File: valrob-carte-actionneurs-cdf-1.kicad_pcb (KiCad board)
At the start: 4 copper layers, 50 x 50 mm, 126 parts, among them J1 USB_C_Receptacle_USB2.0_14P, J2 Conn_01x02, J3 Conn_01x02, J4 Conn_01x04_Pin, J5 Conn_01x02, J6 Conn_01x02, J7 Conn_01x12, M1 Motor_Servo, M10 Motor_Servo, M11 Motor_Servo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

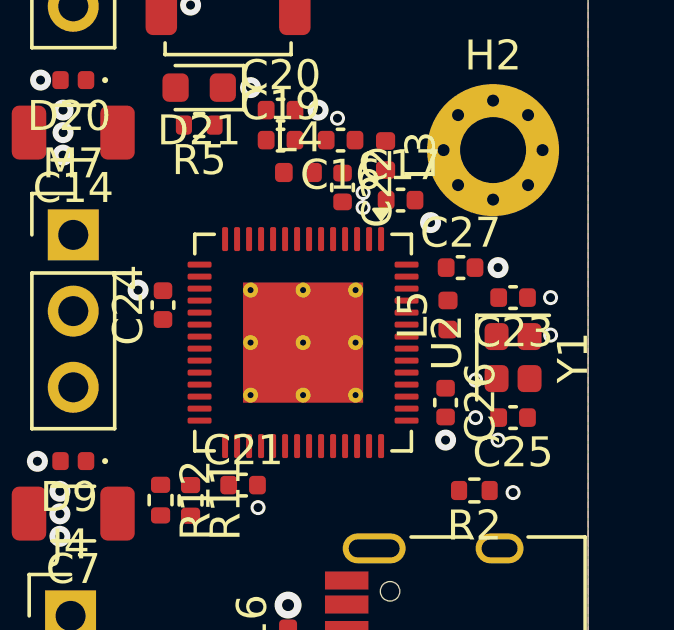
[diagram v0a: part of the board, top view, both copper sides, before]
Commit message: schem: reorganize programmable GPIOs
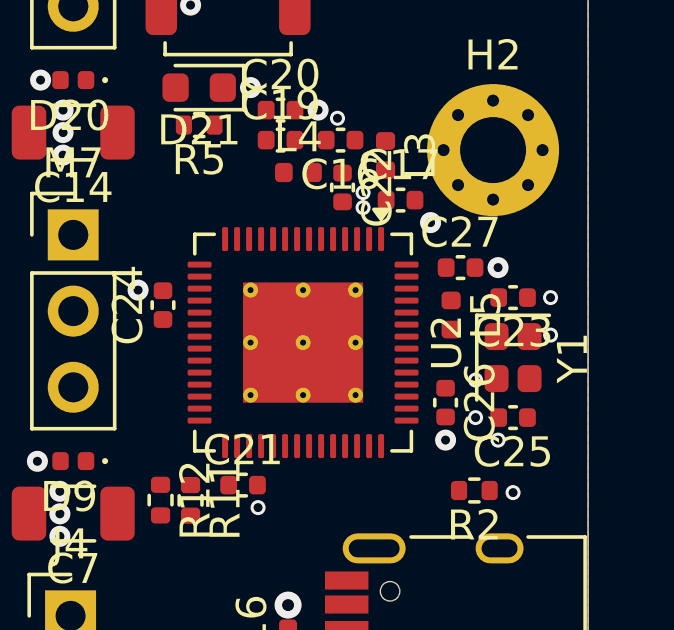
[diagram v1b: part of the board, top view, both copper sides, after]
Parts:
- moved L5 0.10 mm to (129.4, 76.3), turned to -90 degrees
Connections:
- J7 pad 1: /GPIO41 -> /GPIO48
- J7 pad 10: /GPIO15 -> /GPIO40
- J7 pad 11: /GPIO16 -> /GPIO41
- J7 pad 2: /GPIO42 -> /GPIO47
- J7 pad 8: /GPIO47 -> /GPIO38
- J7 pad 9: /GPIO48 -> /GPIO39
- U2 pad 10: /PG_B -> /SERVO10
- U2 pad 11: /SERVO1 -> /SERVO9
- U2 pad 12: /SERVO2 -> /SERVO8
- U2 pad 13: /SERVO3 -> /SERVO6
- U2 pad 14: /SERVO4 -> /SERVO7
- U2 pad 16: /SERVO6 -> /SERVO4
- U2 pad 17: /SERVO7 -> /SERVO3
- U2 pad 18: /SERVO8 -> /SERVO2
- U2 pad 19: /SERVO9 -> /SERVO1
- U2 pad 21: /GPIO15 -> /PG_B
- U2 pad 22: /GPIO16 -> /PG_A
- U2 pad 23: /SERVO10 -> /ILM_A
- U2 pad 24: /SERVO11 -> /ILM_B
- U2 pad 27: /SERVO12 -> /RGB
- U2 pad 43: /SERVO13 -> /GPIO38
- U2 pad 44: /CAN_TX -> /GPIO39
- U2 pad 45: /CAN_RX -> /GPIO40
- U2 pad 48: /GPIO42 -> /CAN_RX
- U2 pad 51: /SERVO14 -> /CAN_TX
- U2 pad 6: /RGB -> /SERVO14
- U2 pad 7: /ILM_A -> /SERVO13
- U2 pad 8: /ILM_B -> /SERVO12
- U2 pad 9: /PG_A -> /SERVO11

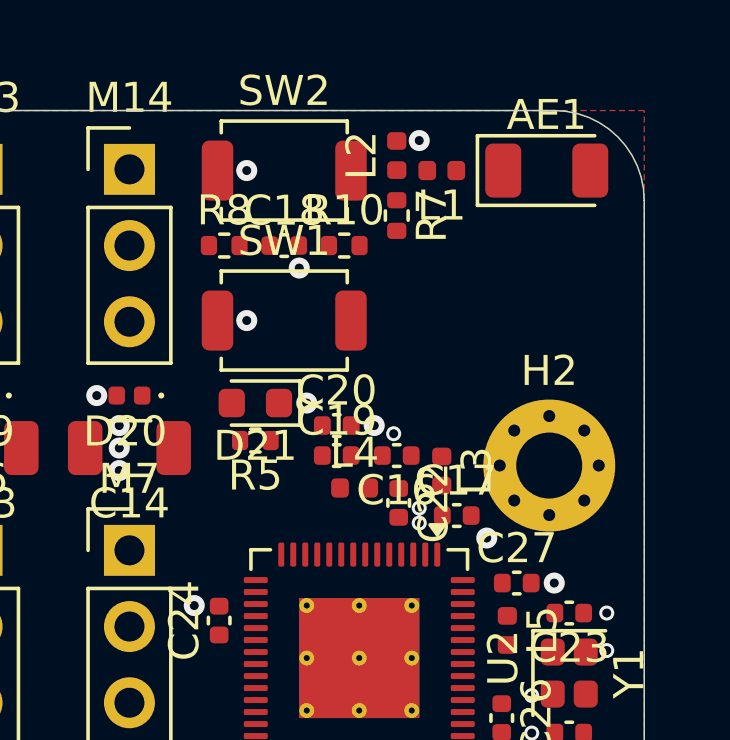
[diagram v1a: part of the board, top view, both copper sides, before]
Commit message: pcb: add rf routing
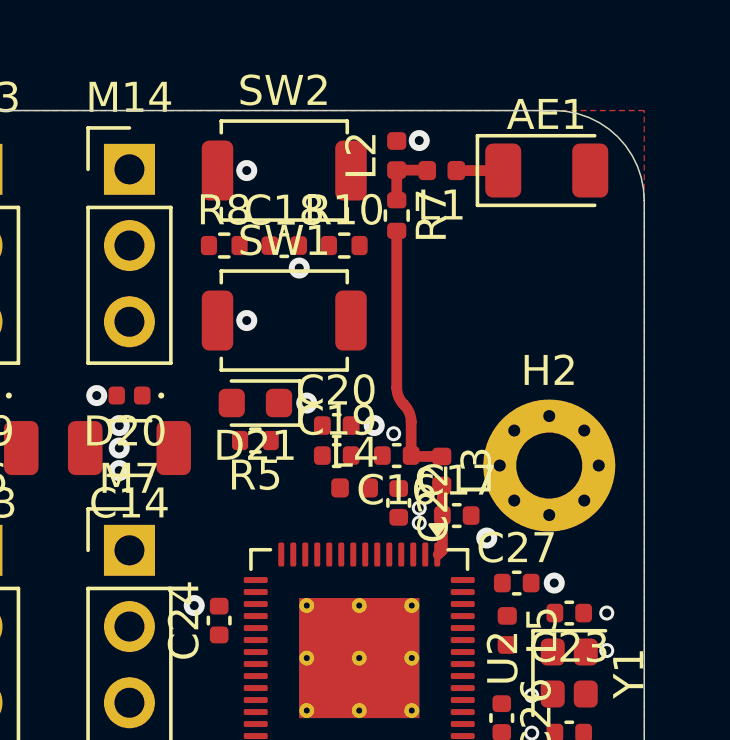
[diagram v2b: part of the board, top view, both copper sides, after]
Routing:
- net /RF_TRANS: track 0.00 -> 8.64 mm
- net /RF_ESP: track 0.00 -> 2.37 mm
- net Net-(L1-Pad2): track 0.00 -> 2.03 mm
- net /RF_ANT: track 0.00 -> 1.57 mm
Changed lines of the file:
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@@
 		(layer "Edge.Cuts")
 	)
+	(segment
+		(start 127.735 61)
+		(end 129.3 61)
+		(width 0.359)
+		(layer "F.Cu")
+		(net 1)
+	)
 	(via
 		(at 106.25 90.25)
@@
 		(net 2)
 	)
+	(segment
+		(start 126.23 70.5)
+		(end 126.23 69.376371)
+		(width 0.359)
+		(layer "F.Cu")
+		(net 4)
+	)
+	(segment
+		(start 126.26 70.53)
+		(end 126.23 70.5)
+		(width 0.359)
+		(layer "F.Cu")
+		(net 4)
+	)
+	(segment
+		(start 125.995685 68.810685)
+		(end 125.984314 68.799314)
+		(width 0.359)
+		(layer "F.Cu")
+		(net 4)
+	)
+	(segment
+		(start 127.25 70.53)
+		(end 126.26 70.53)
+		(width 0.359)
+		(layer "F.Cu")
+		(net 4)
+	)
+	(segment
+		(start 125.75 68.233629)
+		(end 125.75 63.01)
+		(width 0.359)
+		(layer "F.Cu")
+		(net 4)
+	)
+	(arc
+		(start 125.984314 68.799314)
+		(mid 125.810896 68.539775)
+		(end 125.75 68.233629)
+		(width 0.359)
+		(layer "F.Cu")
+		(net 4)
+	)
+	(arc
+		(start 126.23 69.376371)
+		(mid 126.169103 69.070224)
+		(end 125.995685 68.810685)
+		(width 0.359)
+		(layer "F.Cu")
+		(net 4)
+	)
+	(segment
+		(start 127.27 73.6605)
+		(end 127.1305 73.8)
+		(width 0.359)
+		(layer "F.Cu")
+		(net 5)
+	)
+	(segment
+		(start 127.27 71.52)
+		(end 127.25 71.5)
+		(width 0.359)
+		(layer "F.Cu")
+		(net 5)
+	)
+	(segment
+		(start 127.27 72.5)
+		(end 127.27 71.52)
+		(width 0.359)
+		(layer "F.Cu")
+		(net 5)
+	)
+	(segment
+		(start 127.27 72.5)
+		(end 127.27 73.6605)
+		(width 0.359)
+		(layer "F.Cu")
+		(net 5)
+	)
+	(segment
+		(start 126.75 60.985)
+		(end 126.765 61)
+		(width 0.359)
+		(layer "F.Cu")
+		(net 34)
+	)
+	(segment
+		(start 125.75 61.99)
+		(end 125.75 60.985)
+		(width 0.359)
+		(layer "F.Cu")
+		(net 34)
+	)
+	(segment
+		(start 125.75 60.985)
+		(end 126.75 60.985)
+		(width 0.359)
+		(layer "F.Cu")
+		(net 34)
+	)
 	(zone

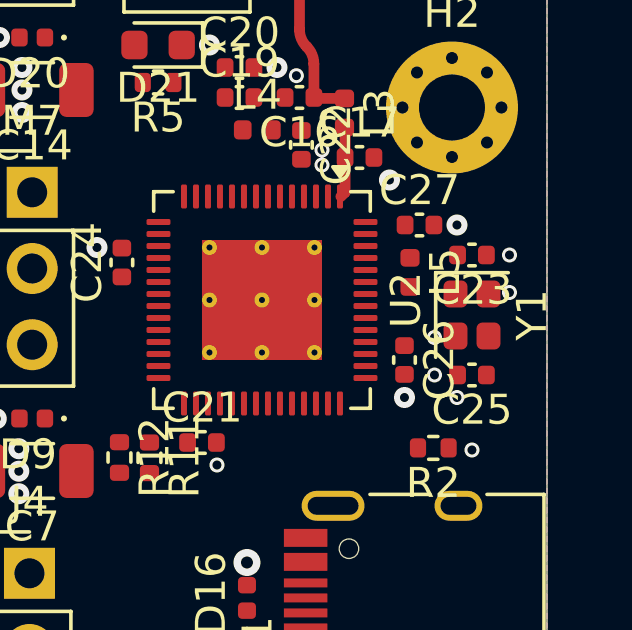
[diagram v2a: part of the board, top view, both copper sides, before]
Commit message: pcb: add crystal routing
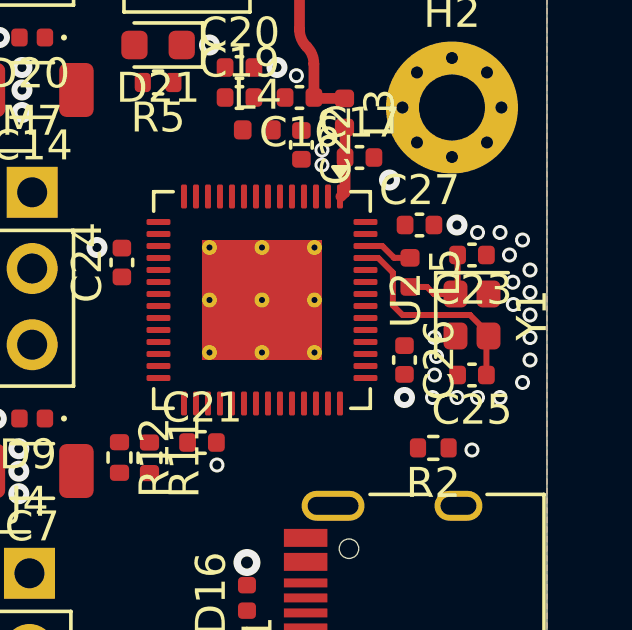
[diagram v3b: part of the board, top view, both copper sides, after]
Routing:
- net /XTAL_N: track 0.00 -> 7.20 mm
- net /XTAL_PL: track 0.00 -> 2.94 mm
- net /XTAL_P: track 0.00 -> 1.65 mm
- net GND: vias 121 -> 135

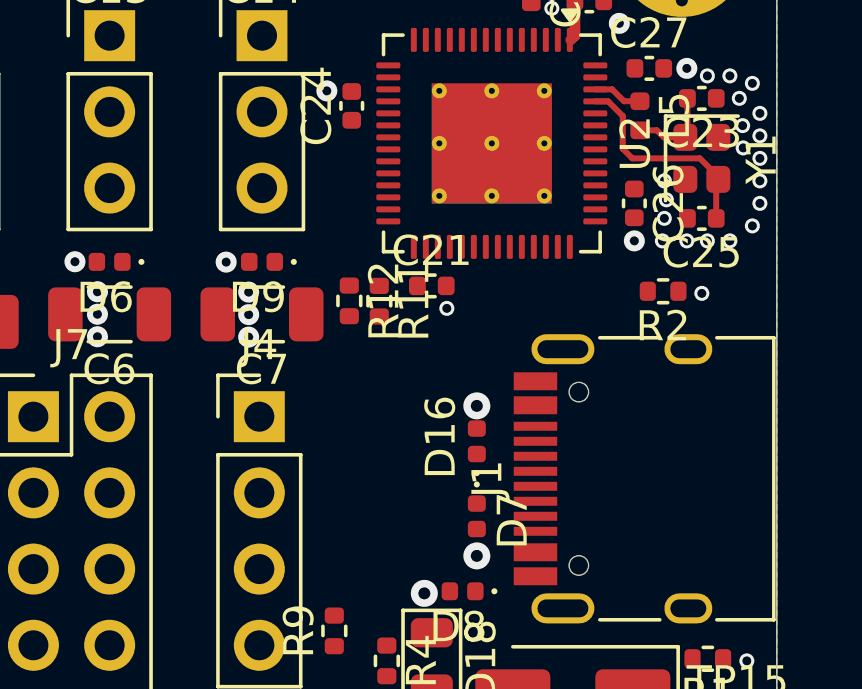
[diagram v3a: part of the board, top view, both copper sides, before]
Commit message: pcb: add usb routing
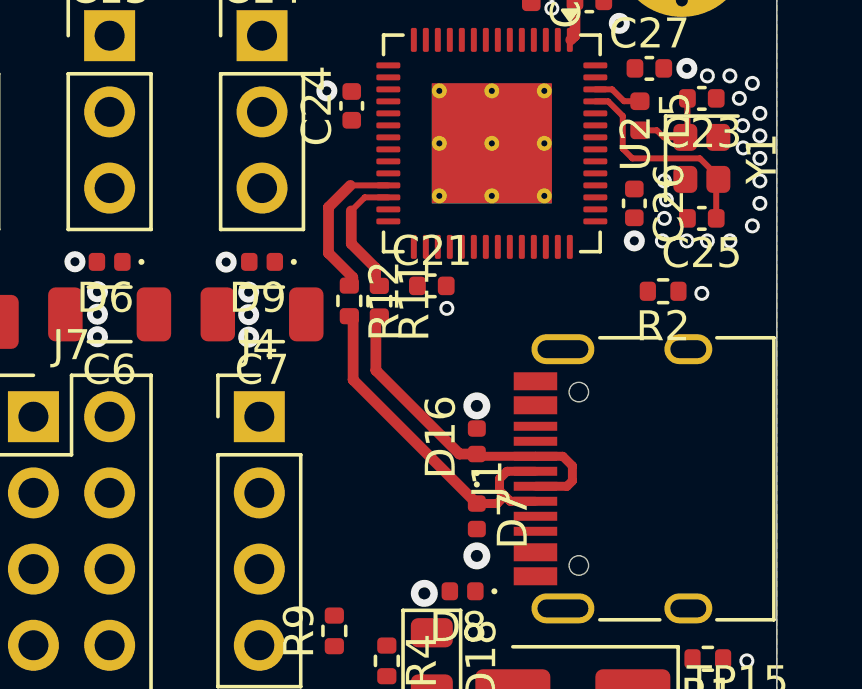
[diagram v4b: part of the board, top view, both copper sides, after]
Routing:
- net /D-: track 0.00 -> 12.1 mm
- net /D+: track 0.00 -> 11.5 mm
- net /ESP_D-: track 0.00 -> 5.29 mm
- net /ESP_D+: track 0.00 -> 4.31 mm

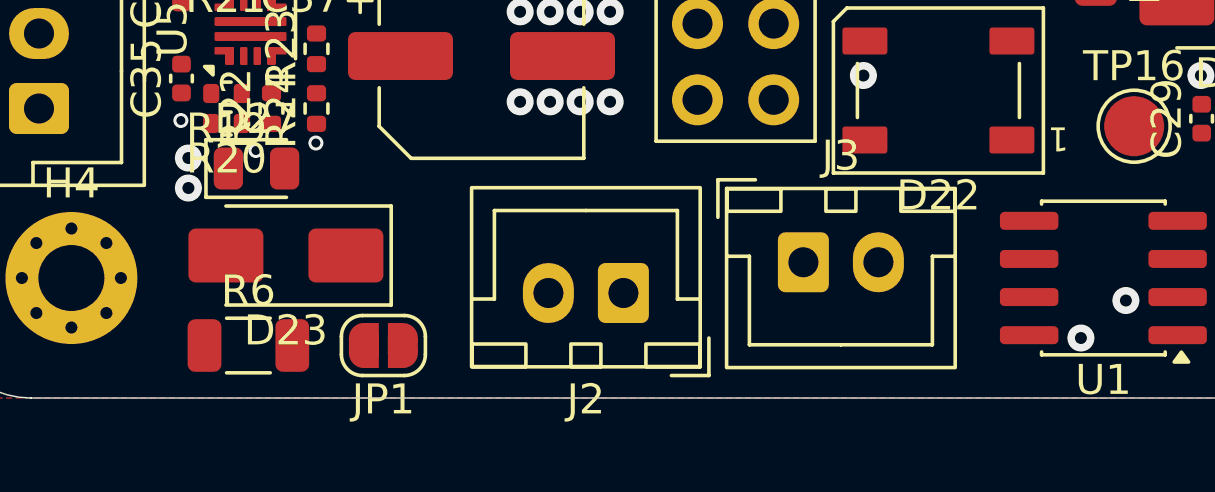
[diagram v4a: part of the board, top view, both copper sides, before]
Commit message: pcb: add can routing
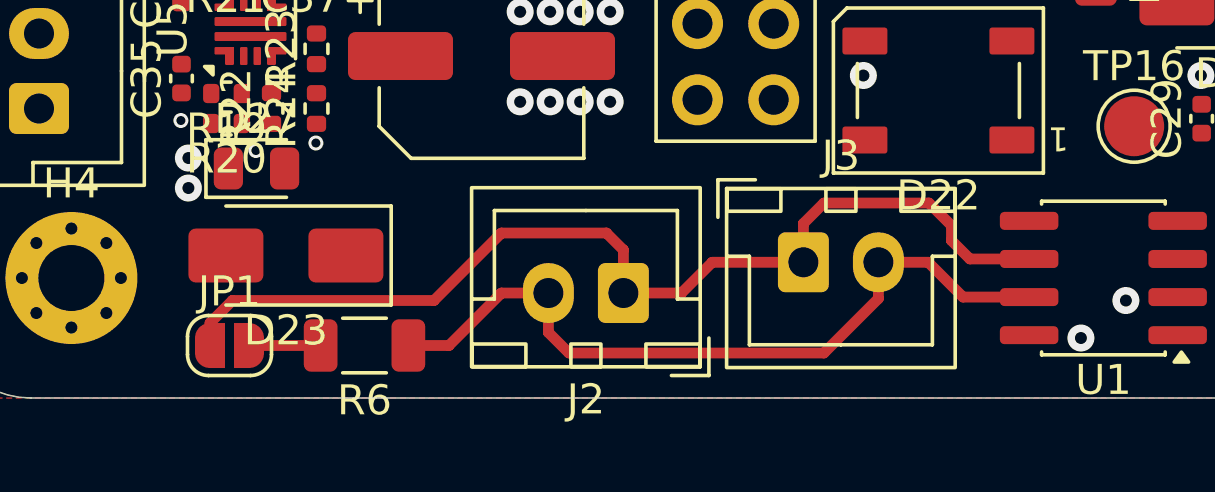
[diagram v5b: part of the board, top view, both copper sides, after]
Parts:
- moved JP1 5.13 mm to (93.6, 107.2), turned to 0 degrees
- moved R6 3.87 mm to (98.1, 107.2), turned to 180 degrees
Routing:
- net /CANL: track 0.00 -> 34.0 mm
- net /CANH: track 0.00 -> 25.5 mm
- net Net-(JP1-B): track 0.00 -> 2.39 mm

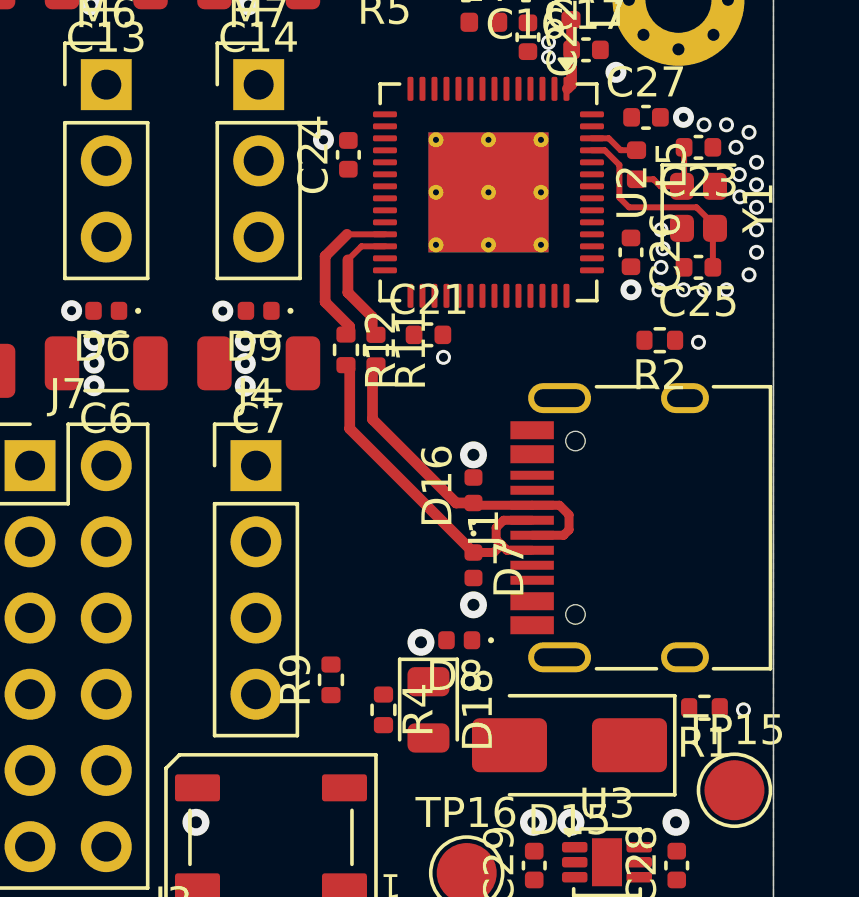
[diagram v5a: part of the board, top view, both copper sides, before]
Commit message: pcb: add UART routing
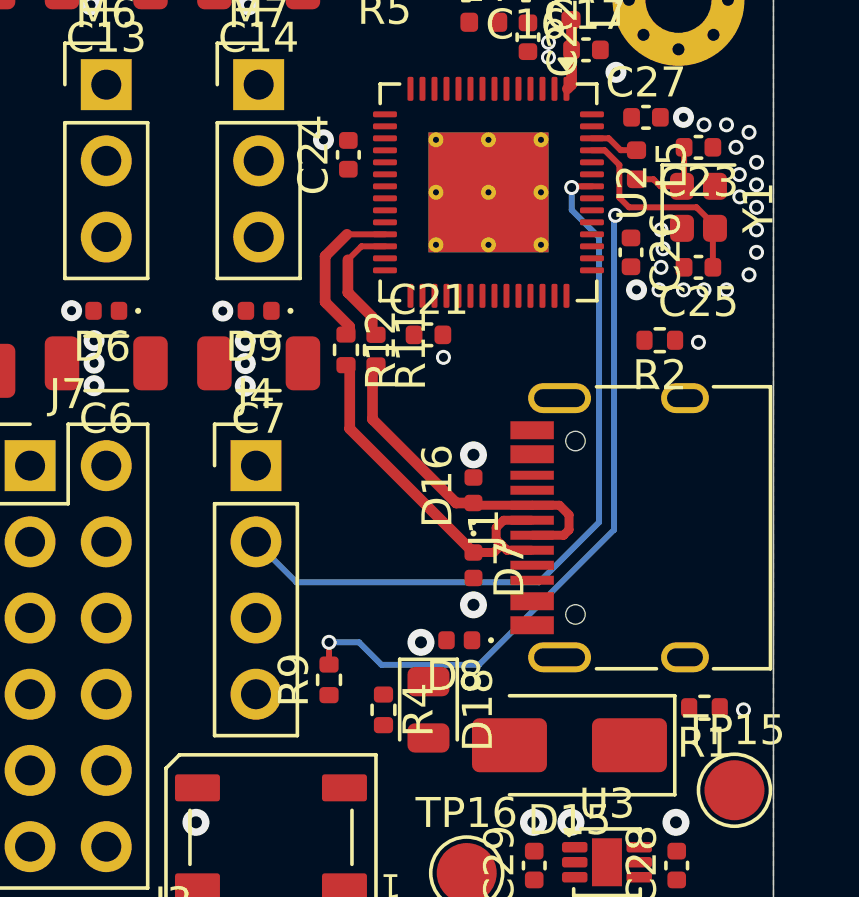
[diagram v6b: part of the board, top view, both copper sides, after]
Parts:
- moved R9 0.06 mm to (119.2, 93.5)
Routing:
- net /U0RXD: track 0.00 -> 25.1 mm, vias 0 -> 1
- net /U0TXD: track 0.00 -> 22.9 mm, vias 0 -> 2

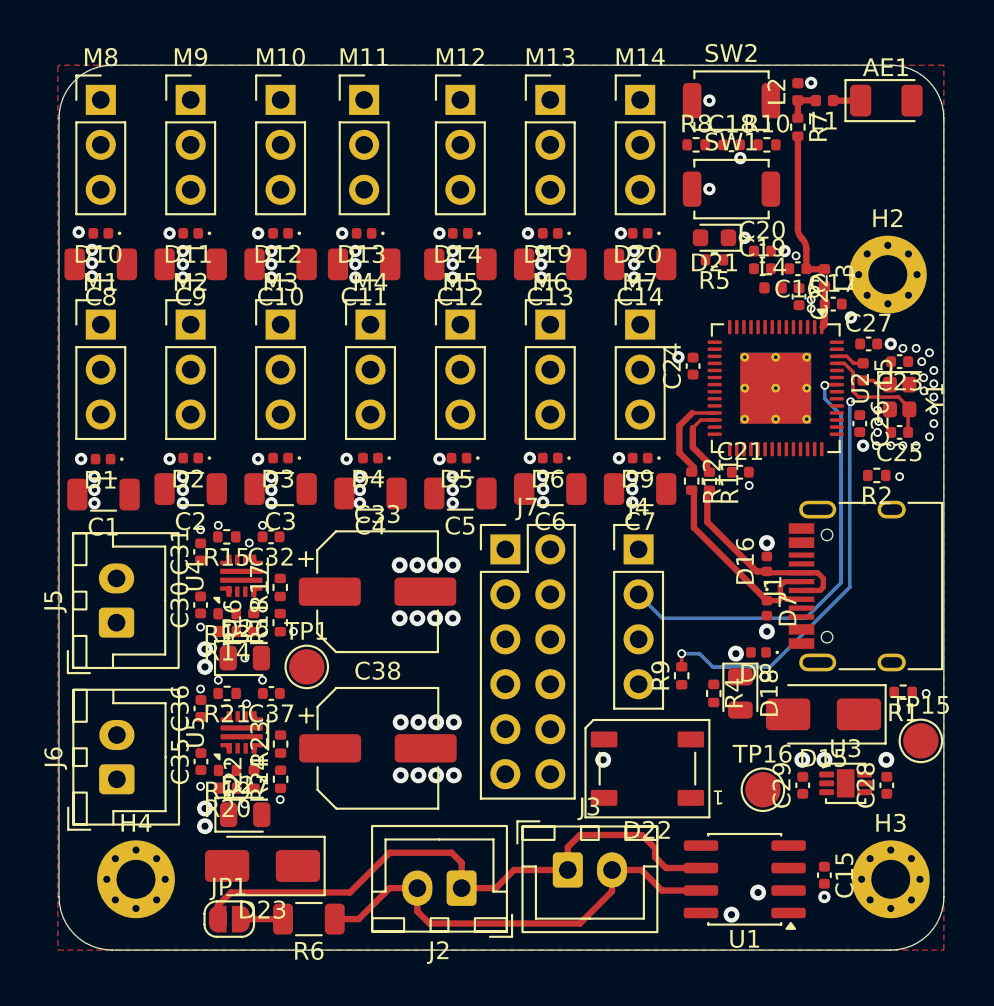
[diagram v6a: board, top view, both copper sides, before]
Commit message: pcb: add servo 5V routing
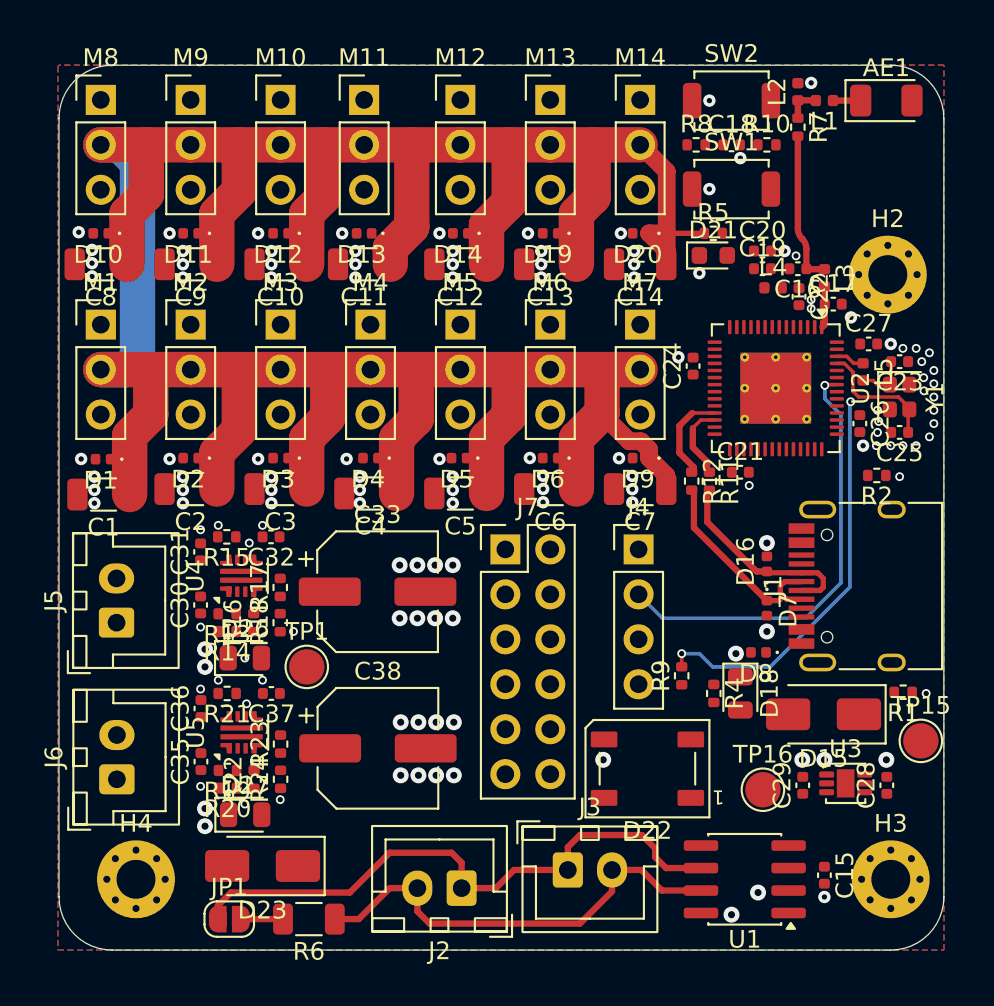
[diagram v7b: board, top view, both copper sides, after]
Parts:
- moved R5 1.50 mm to (121.0, 68.5), turned to 0 degrees
- moved D21 1.00 mm to (121.0, 69.8), turned to 0 degrees
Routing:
- net +5V: track 0.00 -> 182.7 mm
- added copper zone on B.Cu, net GND
- added copper zone on In1.Cu, net GND
- added copper zone on In2.Cu, net GND
